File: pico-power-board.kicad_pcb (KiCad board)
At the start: 2 copper layers, 120 x 70 mm, 114 parts, among them J1 Conn_02x10_Counter_Clockwise, J10 Conn_01x20_Female, J2 Conn_02x10_Counter_Clockwise, J3 Conn_02x10_Counter_Clockwise, J4 Conn_02x10_Counter_Clockwise, J5 Conn_02x10_Counter_Clockwise, J6 Conn_02x10_Counter_Clockwise, J7 DC-042C-Z-2.5, J8 Conn_01x06_Male, J9 Conn_01x20_Female, U1 TMP112AIDRLR, U2 INA219AxD, U3 K7803-500R3, U4 74LVC1G125GW,125, U5 74LVC1G125GW,125, U6 74LVC1G125GW,125, U7 74LVC1G125GW,125, U8 74LVC1G125GW,125, U9 74LVC1G125GW,125

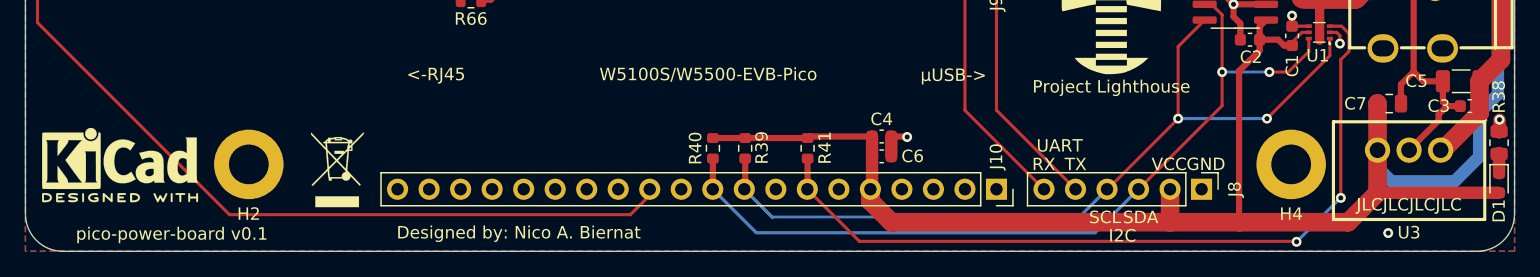
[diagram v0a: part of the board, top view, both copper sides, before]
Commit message: Fix wrong resistor 100k -> 100R, add teardrops, larger resistor to dim power led
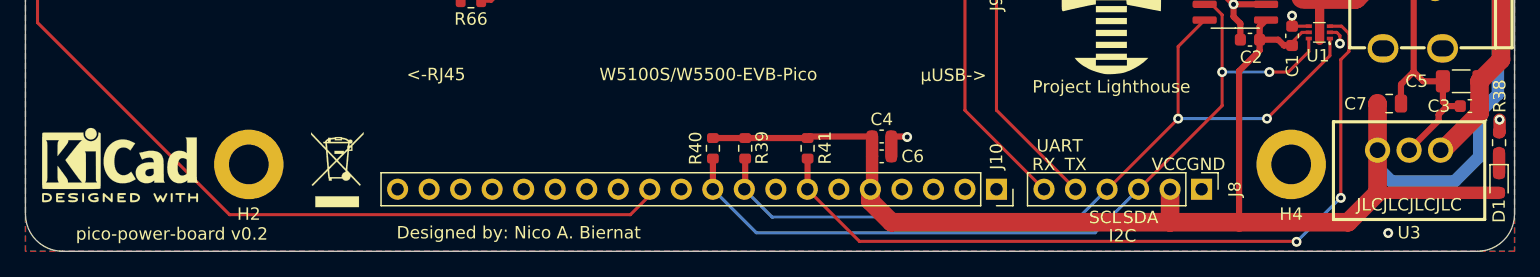
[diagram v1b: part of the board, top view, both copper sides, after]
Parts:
- R1, R10, R11, R12, R19, R2, R20, R21, R22, R23, R24, R25, R26, R27, R28, R29, R3, R30, R4, R5, R54, R55, R56, R57, R58, R59, R6, R7, R8, R9: value 100 -> 100R
- R38: value 470 -> 1k; footprint Resistor_SMD:R_0805_2012Metric -> Resistor_SMD:R_0603_1608Metric
- R42, R43, R44, R45, R46, R47, R48, R49, R50, R51, R52, R53: value 200 -> 200R
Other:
- board text added: "pico-power-board v0.2"
- board text removed: "TODO: - maybe put Pico higher so it doesn't cover the screw"
- board text removed: "pico-power-board v0.1"

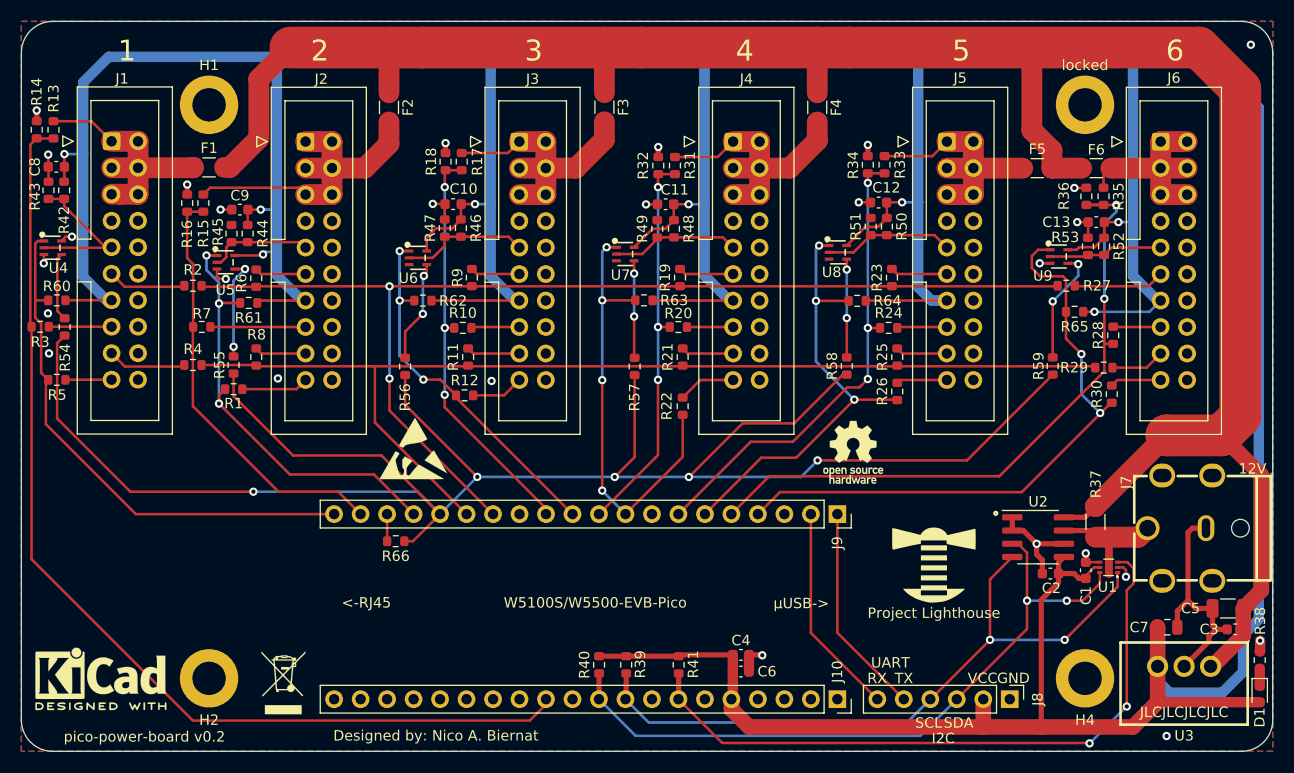
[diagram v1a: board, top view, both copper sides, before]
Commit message: Move pico down in order to not interfere with the case on the backside
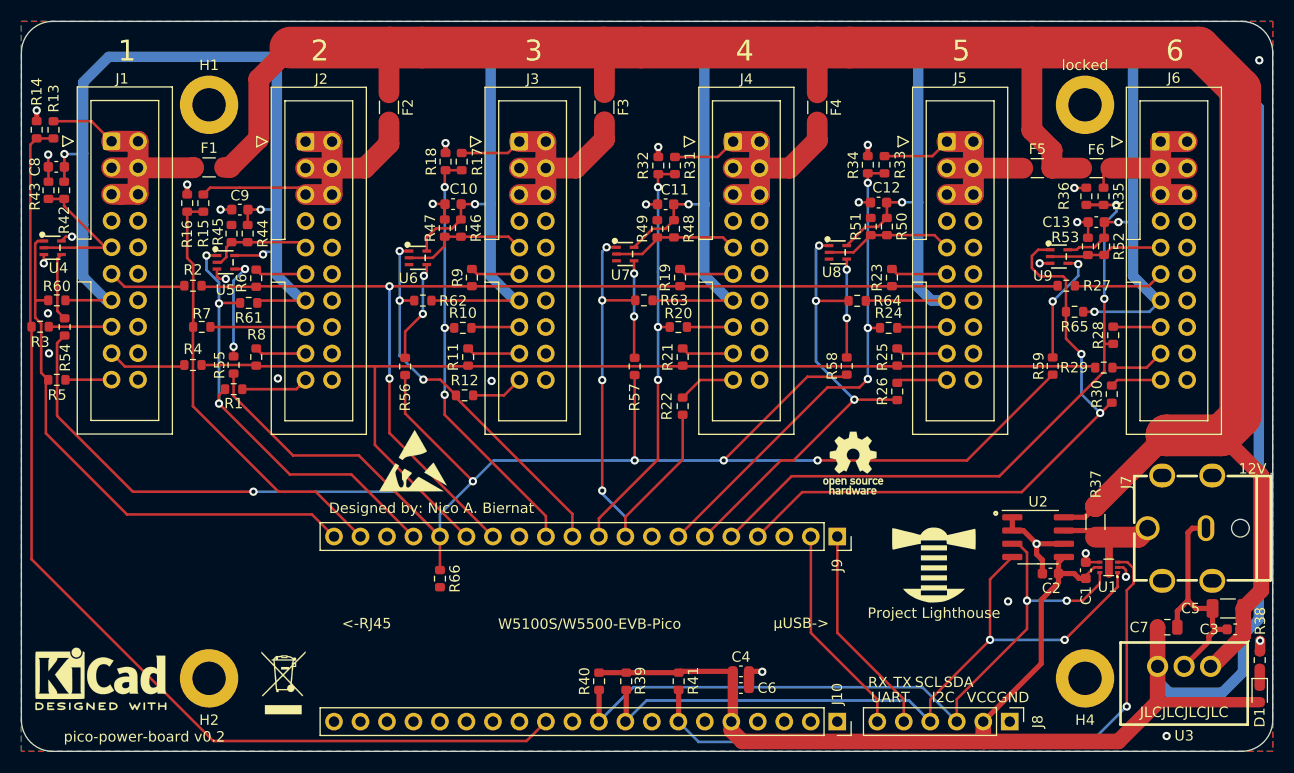
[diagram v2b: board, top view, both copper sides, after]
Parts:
- moved R66 5.56 mm to (130.1, 128.4), turned to -90 degrees
- moved J10 2.15 mm to (168.2, 142.2)
- moved J9 2.15 mm to (168.2, 124.4)
- moved J8 2.15 mm to (184.8, 142.2)
- moved C4 1.58 mm to (159.0, 137.3)
- moved C6 1.58 mm to (159.0, 138.9)
- moved R39 1.58 mm to (148.0, 138.3)
- moved R40 1.58 mm to (145.4, 138.3)
- moved R41 1.58 mm to (153.0, 138.3)
- moved REF_ESD 1.17 mm to (127.6, 117.1)
- moved REF_OSH 1.03 mm to (169.8, 117.4)
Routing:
- net CS4: track 42.6 -> 46.9 mm
- net MISO: track 186.6 -> 183.0 mm
- net GND: track 63.1 -> 60.5 mm, vias 26 -> 27
- net I2C_SDA: track 67.0 -> 69.6 mm
- net I2C_SCL: track 66.2 -> 68.7 mm
- net SCK: track 108.2 -> 110.3 mm
- net RESET3: track 39.5 -> 41.6 mm
- net MOSI: track 103.1 -> 105.3 mm
- net CS3: track 35.4 -> 37.5 mm
- net RESET4: track 37.8 -> 39.8 mm
- net +3V3: track 523.2 -> 525.1 mm
- net CS1: track 51.3 -> 52.7 mm
- net CS5: track 43.5 -> 44.4 mm
- net CS6: track 59.4 -> 60.3 mm
- net RESET6: track 63.3 -> 64.2 mm
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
